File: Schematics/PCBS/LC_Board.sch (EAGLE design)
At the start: 21 parts, among them IC1 ATMEGA328P-AU, Q1 TRANSISTOR-FET_DMN2004K, Q10 220mA/50V/3.5Ω, Q2 TRANSISTOR-FET_DMN2004K, Q3 TRANSISTOR-FET_DMN2004K, Q4 TRANSISTOR-FET_DMN2004K, Q5 TRANSISTOR-FET_DMN2004K, Q6 TRANSISTOR-FET_DMN2004K, Q7 TRANSISTOR-FET_DMN2004K, Q8 TRANSISTOR-FET_DMN2004K, Q9 TRANSISTOR-FET_DMN2004K, U1 LT1763CS8-3.3#TRPBF

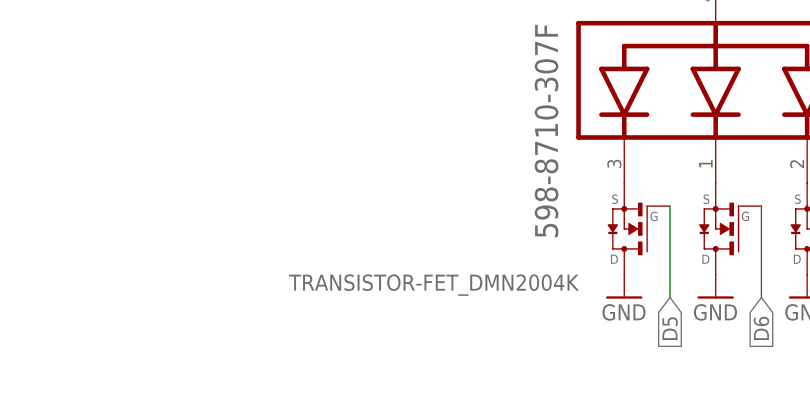
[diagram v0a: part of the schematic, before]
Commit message: update .gitignore && added MOSFET value to board
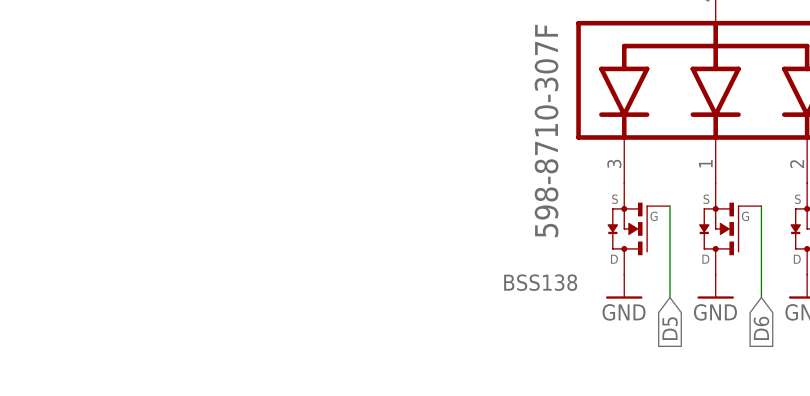
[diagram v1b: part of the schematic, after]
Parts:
- Q1, Q2, Q3, Q4, Q5, Q6, Q7, Q8, Q9: value TRANSISTOR-FET_DMN2004K -> BSS138
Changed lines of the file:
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@@
 <attribute name="SPICEPREFIX" value="E"/>
 </part>
-<part name="Q1" library="52101-101-REV-A" library_urn="urn:adsk.eagle:library:15662110" deviceset="TRANSISTOR-FET_DMN2004K" device="" package3d_urn="urn:adsk.eagle:package:15662287/2">
+<part name="Q1" library="52101-101-REV-A" library_urn="urn:adsk.eagle:library:15662110" deviceset="TRANSISTOR-FET_DMN2004K" device="" package3d_urn="urn:adsk.eagle:package:15662287/2" value="BSS138">
 <attribute name="SPICEPREFIX" value="Q"/>
 </part>
-<part name="Q2" library="52101-101-REV-A" library_urn="urn:adsk.eagle:library:15662110" deviceset="TRANSISTOR-FET_DMN2004K" device="" package3d_urn="urn:adsk.eagle:package:15662287/2">
+<part name="Q2" library="52101-101-REV-A" library_urn="urn:adsk.eagle:library:15662110" deviceset="TRANSISTOR-FET_DMN2004K" device="" package3d_urn="urn:adsk.eagle:package:15662287/2" value="BSS138">
 <attribute name="SPICEPREFIX" value="Q"/>
 </part>
-<part name="Q3" library="52101-101-REV-A" library_urn="urn:adsk.eagle:library:15662110" deviceset="TRANSISTOR-FET_DMN2004K" device="" package3d_urn="urn:adsk.eagle:package:15662287/2">
+<part name="Q3" library="52101-101-REV-A" library_urn="urn:adsk.eagle:library:15662110" deviceset="TRANSISTOR-FET_DMN2004K" device="" package3d_urn="urn:adsk.eagle:package:15662287/2" value="BSS138">
 <attribute name="SPICEPREFIX" value="Q"/>
 </part>
-<part name="Q4" library="52101-101-REV-A" library_urn="urn:adsk.eagle:library:15662110" deviceset="TRANSISTOR-FET_DMN2004K" device="" package3d_urn="urn:adsk.eagle:package:15662287/2">
+<part name="Q4" library="52101-101-REV-A" library_urn="urn:adsk.eagle:library:15662110" deviceset="TRANSISTOR-FET_DMN2004K" device="" package3d_urn="urn:adsk.eagle:package:15662287/2" value="BSS138">
 <attribute name="SPICEPREFIX" value="Q"/>
 </part>
-<part name="Q5" library="52101-101-REV-A" library_urn="urn:adsk.eagle:library:15662110" deviceset="TRANSISTOR-FET_DMN2004K" device="" package3d_urn="urn:adsk.eagle:package:15662287/2">
+<part name="Q5" library="52101-101-REV-A" library_urn="urn:adsk.eagle:library:15662110" deviceset="TRANSISTOR-FET_DMN2004K" device="" package3d_urn="urn:adsk.eagle:package:15662287/2" value="BSS138">
 <attribute name="SPICEPREFIX" value="Q"/>
 </part>
-<part name="Q6" library="52101-101-REV-A" library_urn="urn:adsk.eagle:library:15662110" deviceset="TRANSISTOR-FET_DMN2004K" device="" package3d_urn="urn:adsk.eagle:package:15662287/2">
+<part name="Q6" library="52101-101-REV-A" library_urn="urn:adsk.eagle:library:15662110" deviceset="TRANSISTOR-FET_DMN2004K" device="" package3d_urn="urn:adsk.eagle:package:15662287/2" value="BSS138">
 <attribute name="SPICEPREFIX" value="Q"/>
 </part>
-<part name="Q7" library="52101-101-REV-A" library_urn="urn:adsk.eagle:library:15662110" deviceset="TRANSISTOR-FET_DMN2004K" device="" package3d_urn="urn:adsk.eagle:package:15662287/2">
+<part name="Q7" library="52101-101-REV-A" library_urn="urn:adsk.eagle:library:15662110" deviceset="TRANSISTOR-FET_DMN2004K" device="" package3d_urn="urn:adsk.eagle:package:15662287/2" value="BSS138">
 <attribute name="SPICEPREFIX" value="Q"/>
 </part>
-<part name="Q8" library="52101-101-REV-A" library_urn="urn:adsk.eagle:library:15662110" deviceset="TRANSISTOR-FET_DMN2004K" device="" package3d_urn="urn:adsk.eagle:package:15662287/2">
+<part name="Q8" library="52101-101-REV-A" library_urn="urn:adsk.eagle:library:15662110" deviceset="TRANSISTOR-FET_DMN2004K" device="" package3d_urn="urn:adsk.eagle:package:15662287/2" value="BSS138">
 <attribute name="SPICEPREFIX" value="Q"/>
 </part>
-<part name="Q9" library="52101-101-REV-A" library_urn="urn:adsk.eagle:library:15662110" deviceset="TRANSISTOR-FET_DMN2004K" device="" package3d_urn="urn:adsk.eagle:package:15662287/2">
+<part name="Q9" library="52101-101-REV-A" library_urn="urn:adsk.eagle:library:15662110" deviceset="TRANSISTOR-FET_DMN2004K" device="" package3d_urn="urn:adsk.eagle:package:15662287/2" value="BSS138">
 <attribute name="SPICEPREFIX" value="Q"/>
 </part>

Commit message: updated IO
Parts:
- JP1: device adafruit:PINHD-1X8CLEANBIG -> pinhead:PINHD-1X8
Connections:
- new net RESET_IN: JP1.5
- net 2BD: no longer JP1.2
- net 3.3V_RAIL: now also JP1.4; no longer JP1.5
- net 5V_RAIL: now also JP1.3; no longer JP1.6
- net RXD_IN: now also JP1.6; no longer JP1.3
- net TXD: now also JP1.7; no longer JP1.4
- net VIN: now also JP1.2; no longer JP1.7
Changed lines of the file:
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@@
 <part name="R3" library="SparkFun-Resistors" deviceset="10OHM" device="-HORIZ-1/4W-1%" value="10K"/>
 <part name="Q10" library="SparkFun-DiscreteSemi" deviceset="MOSFET-NCH" device="-BSS138" value="220mA/50V/3.5Ω"/>
-<part name="JP1" library="adafruit" library_urn="urn:adsk.eagle:library:420" deviceset="PINHD-1X8" device="CLEANBIG" package3d_urn="urn:adsk.eagle:package:6240708/1"/>
 <part name="E1" library="52101-101-REV-A" library_urn="urn:adsk.eagle:library:15662110" deviceset="DPADS_PAD" device="-0400-S" package3d_urn="urn:adsk.eagle:package:15662248/2"/>
 <part name="E2" library="52101-101-REV-A" library_urn="urn:adsk.eagle:library:15662110" deviceset="DPADS_PAD" device="-0400-S" package3d_urn="urn:adsk.eagle:package:15662248/2"/>
+<part name="JP1" library="pinhead" library_urn="urn:adsk.eagle:library:325" deviceset="PINHD-1X8" device="" package3d_urn="urn:adsk.eagle:package:22409/2"/>
 </parts>
 <sheets>
@@
 </instance>
 <instance part="Q10" gate="NMOS" x="452.12" y="2.54" smashed="yes" rot="R90"/>
-<instance part="JP1" gate="G$1" x="449.58" y="30.48" smashed="yes" rot="R180">
+<instance part="E1" gate="P" x="558.8" y="33.02" smashed="yes" rot="R180">
+<attribute name="NAME" x="556.895" y="33.9725" size="1.778" layer="95" rot="R180"/>
+</instance>
+<instance part="E2" gate="P" x="558.8" y="30.48" smashed="yes" rot="R180">
+<attribute name="NAME" x="556.895" y="31.4325" size="1.778" layer="95" rot="R180"/>
+</instance>
+<instance part="JP1" gate="A" x="449.58" y="33.02" smashed="yes" rot="R180">
 <attribute name="NAME" x="455.93" y="19.685" size="1.778" layer="95" rot="R180"/>
 <attribute name="VALUE" x="455.93" y="45.72" size="1.778" layer="96" rot="R180"/>
-</instance>
-<instance part="E1" gate="P" x="558.8" y="33.02" smashed="yes" rot="R180">
-<attribute name="NAME" x="556.895" y="33.9725" size="1.778" layer="95" rot="R180"/>
-</instance>
-<instance part="E2" gate="P" x="558.8" y="30.48" smashed="yes" rot="R180">
-<attribute name="NAME" x="556.895" y="31.4325" size="1.778" layer="95" rot="R180"/>
 </instance>
 </instances>
@@
 </segment>
 <segment>
-<wire x1="452.12" y1="33.02" x2="457.2" y2="33.02" width="0.1524" layer="91"/>
-<label x="457.2" y="33.02" size="0.5588" layer="95" xref="yes"/>
-<pinref part="JP1" gate="G$1" pin="5"/>
+<wire x1="452.12" y1="30.48" x2="457.2" y2="30.48" width="0.1524" layer="91"/>
+<label x="457.2" y="30.48" size="0.5588" layer="95" xref="yes"/>
+<pinref part="JP1" gate="A" pin="4"/>
 </segment>
 </net>
@@
 <pinref part="GND18" gate="1" pin="GND"/>
 <wire x1="452.12" y1="40.64" x2="459.74" y2="40.64" width="0.1524" layer="91"/>
-<pinref part="JP1" gate="G$1" pin="8"/>
+<pinref part="JP1" gate="A" pin="8"/>
 </segment>
 <segment>
@@
 <net name="VIN" class="0">
 <segment>
-<wire x1="452.12" y1="38.1" x2="457.2" y2="38.1" width="0.1524" layer="91"/>
-<label x="457.2" y="38.1" size="0.6096" layer="95" xref="yes"/>
-<pinref part="JP1" gate="G$1" pin="7"/>
+<wire x1="452.12" y1="25.4" x2="457.2" y2="25.4" width="0.1524" layer="91"/>
+<label x="457.2" y="25.4" size="0.6096" layer="95" xref="yes"/>
+<pinref part="JP1" gate="A" pin="2"/>
 </segment>
 <segment>
@@
 </segment>
 <segment>
-<wire x1="452.12" y1="30.48" x2="457.2" y2="30.48" width="0.1524" layer="91"/>
-<label x="457.2" y="30.48" size="0.6096" layer="95" xref="yes"/>
-<pinref part="JP1" gate="G$1" pin="4"/>
+<wire x1="452.12" y1="38.1" x2="457.2" y2="38.1" width="0.1524" layer="91"/>
+<label x="457.2" y="38.1" size="0.6096" layer="95" xref="yes"/>
+<pinref part="JP1" gate="A" pin="7"/>
 </segment>
 </net>
@@
 <net name="RXD_IN" class="0">
 <segment>
-<wire x1="452.12" y1="27.94" x2="457.2" y2="27.94" width="0.1524" layer="91"/>
-<label x="457.2" y="27.94" size="0.6096" layer="95" xref="yes"/>
-<pinref part="JP1" gate="G$1" pin="3"/>
+<wire x1="452.12" y1="35.56" x2="457.2" y2="35.56" width="0.1524" layer="91"/>
+<label x="457.2" y="35.56" size="0.6096" layer="95" xref="yes"/>
+<pinref part="JP1" gate="A" pin="6"/>
 </segment>
 <segment>
@@
 <net name="5V_RAIL" class="0">
 <segment>
-<wire x1="452.12" y1="35.56" x2="457.2" y2="35.56" width="0.1524" layer="91"/>
-<label x="457.2" y="35.56" size="0.5588" layer="95" xref="yes"/>
-<pinref part="JP1" gate="G$1" pin="6"/>
+<wire x1="452.12" y1="27.94" x2="457.2" y2="27.94" width="0.1524" layer="91"/>
+<label x="457.2" y="27.94" size="0.5588" layer="95" xref="yes"/>
+<pinref part="JP1" gate="A" pin="3"/>
 </segment>
 </net>
 <net name="2BD" class="0">
-<segment>
-<wire x1="452.12" y1="25.4" x2="457.2" y2="25.4" width="0.1524" layer="91"/>
-<label x="457.2" y="25.4" size="0.5588" layer="95" xref="yes"/>
-<pinref part="JP1" gate="G$1" pin="2"/>
-</segment>
 <segment>
 <wire x1="452.12" y1="22.86" x2="457.2" y2="22.86" width="0.1524" layer="91"/>
 <label x="457.2" y="22.86" size="0.5588" layer="95" xref="yes"/>
-<pinref part="JP1" gate="G$1" pin="1"/>
-</segment>
-</net>
+<pinref part="JP1" gate="A" pin="1"/>
+</segment>
+</net>
+<net name="RESET_IN" class="0">
+<segment>
+<wire x1="452.12" y1="33.02" x2="457.2" y2="33.02" width="0.1524" layer="91"/>
+<label x="457.2" y="33.02" size="0.5588" layer="95" xref="yes"/>
+<pinref part="JP1" gate="A" pin="5"/>
+</segment>
+</net>

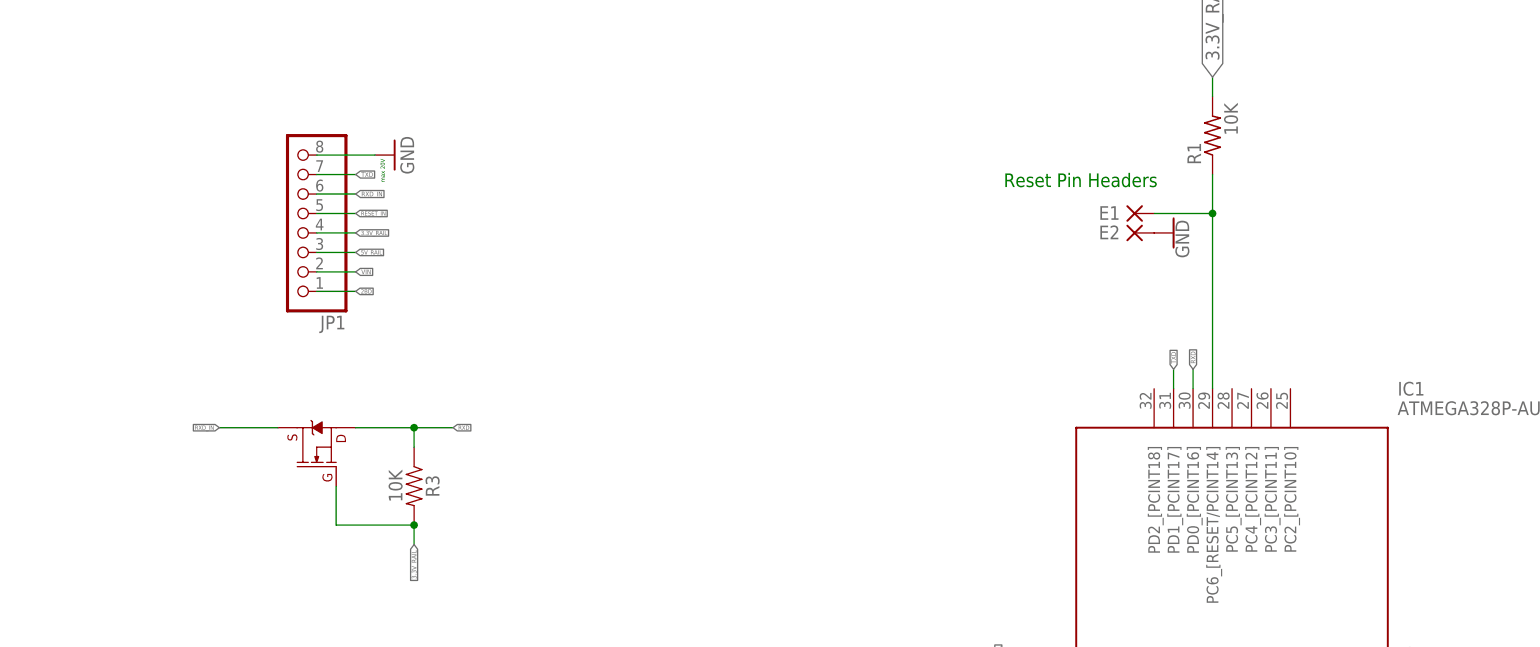
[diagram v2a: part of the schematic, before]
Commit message: 3.3v && 5v selcetor headers added
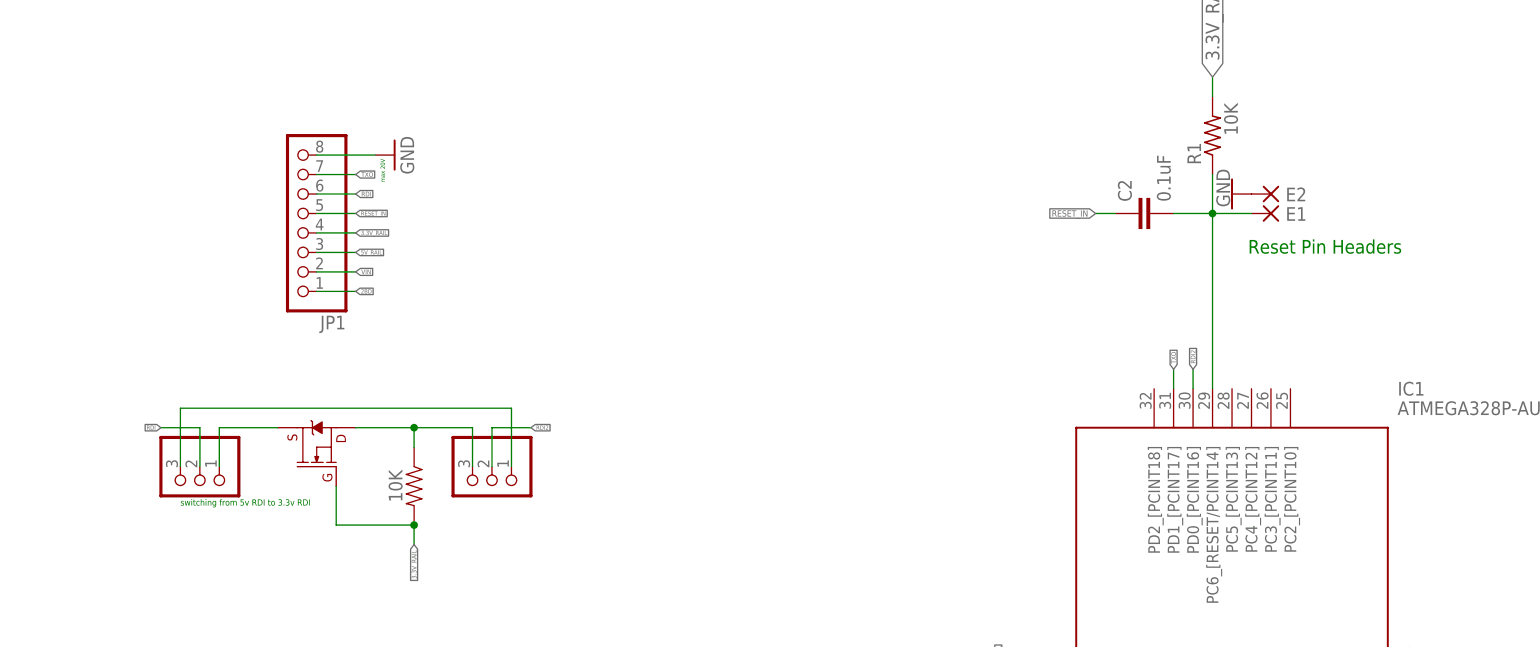
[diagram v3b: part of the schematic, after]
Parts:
- added C2: 0.1uF, SparkFun-Capacitors:0.1UF-0603-25V-(+80/-20%)
- added JP2, JP3: (no value), pinhead:PINHD-1X3
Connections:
- net TXD renamed TXO
- removed net RXD: IC1.PD0_[PCINT16], Q10.S, R3.1
- new net RDI: JP1.6, JP2.2, JP2.3, JP3.1
- new net RDI2: IC1.PD0_[PCINT16], JP3.2
- new net RXI2: JP3.3, Q10.S, R3.1
- net N$15: now also C2.2
- net RESET_IN: now also C2.1
- net RXD_IN: now also JP2.1; no longer JP1.6
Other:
- note added: "switching from 5v RDI to 3.3v RDI"
- moved on the sheet: E1, E2

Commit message: added lables to 5v to 3.3v on RXI
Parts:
- JP1: value (none) -> IO
- JP2: value (none) -> switching from 5v RDI to 3.3v RDI input
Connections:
- new net RDI_3.3V: JP2.3, JP3.1
- net RDI: no longer JP2.3, JP3.1
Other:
- note removed: "switching from 5v RDI to 3.3v RDI"
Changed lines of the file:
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@@
 <part name="E1" library="52101-101-REV-A" library_urn="urn:adsk.eagle:library:15662110" deviceset="DPADS_PAD" device="-0400-S" package3d_urn="urn:adsk.eagle:package:15662248/2"/>
 <part name="E2" library="52101-101-REV-A" library_urn="urn:adsk.eagle:library:15662110" deviceset="DPADS_PAD" device="-0400-S" package3d_urn="urn:adsk.eagle:package:15662248/2"/>
-<part name="JP1" library="pinhead" library_urn="urn:adsk.eagle:library:325" deviceset="PINHD-1X8" device="" package3d_urn="urn:adsk.eagle:package:22409/2"/>
+<part name="JP1" library="pinhead" library_urn="urn:adsk.eagle:library:325" deviceset="PINHD-1X8" device="" package3d_urn="urn:adsk.eagle:package:22409/2" value="IO"/>
 <part name="C2" library="SparkFun-Capacitors" library_urn="urn:adsk.eagle:library:510" deviceset="0.1UF" device="-0603-25V-(+80/-20%)" package3d_urn="urn:adsk.eagle:package:37414/1" value="0.1uF"/>
-<part name="JP2" library="pinhead" library_urn="urn:adsk.eagle:library:325" deviceset="PINHD-1X3" device="" package3d_urn="urn:adsk.eagle:package:22458/2"/>
+<part name="JP2" library="pinhead" library_urn="urn:adsk.eagle:library:325" deviceset="PINHD-1X3" device="" package3d_urn="urn:adsk.eagle:package:22458/2" value="switching from 5v RDI to 3.3v RDI input"/>
 <part name="JP3" library="pinhead" library_urn="urn:adsk.eagle:library:325" deviceset="PINHD-1X3" device="" package3d_urn="urn:adsk.eagle:package:22458/2"/>
 </parts>
@@
 <text x="593.67" y="29.57" size="1.778" layer="91" rot="R180">Reset Pin Headers</text>
 <text x="461.01" y="37.084" size="0.5588" layer="91" rot="R90">max 20V</text>
-<text x="434.34" y="-5.08" size="0.8128" layer="91">switching from 5v RDI to 3.3v RDI</text>
 </plain>
 <instances>
@@
 </instance>
 <instance part="JP1" gate="A" x="449.58" y="33.02" smashed="yes" rot="R180">
-<attribute name="NAME" x="455.93" y="19.685" size="1.778" layer="95" rot="R180"/>
 <attribute name="VALUE" x="455.93" y="45.72" size="1.778" layer="96" rot="R180"/>
 </instance>
@@
 </instance>
 <instance part="JP2" gate="A" x="436.88" y="-2.54" smashed="yes" rot="R270">
-<attribute name="VALUE" x="429.26" y="3.81" size="1.778" layer="96" rot="R270"/>
+<attribute name="VALUE" x="448.31" y="-5.08" size="0.8128" layer="96" rot="R180"/>
 </instance>
 <instance part="JP3" gate="A" x="474.98" y="-2.54" smashed="yes" rot="R270">
@@
 </segment>
 <segment>
-<pinref part="JP2" gate="A" pin="3"/>
-<wire x1="434.34" y1="7.62" x2="434.34" y2="0" width="0.1524" layer="91"/>
-<wire x1="434.34" y1="7.62" x2="477.52" y2="7.62" width="0.1524" layer="91"/>
-<pinref part="JP3" gate="A" pin="1"/>
-<wire x1="477.52" y1="7.62" x2="477.52" y2="0" width="0.1524" layer="91"/>
-</segment>
-<segment>
 <pinref part="JP2" gate="A" pin="2"/>
 <wire x1="436.88" y1="5.08" x2="436.88" y2="0" width="0.1524" layer="91"/>
@@
 </segment>
 </net>
+<net name="RDI_3.3V" class="0">
+<segment>
+<pinref part="JP2" gate="A" pin="3"/>
+<wire x1="434.34" y1="7.62" x2="434.34" y2="0" width="0.1524" layer="91"/>
+<wire x1="434.34" y1="7.62" x2="477.52" y2="7.62" width="0.1524" layer="91"/>
+<pinref part="JP3" gate="A" pin="1"/>
+<wire x1="477.52" y1="7.62" x2="477.52" y2="0" width="0.1524" layer="91"/>
+<label x="434.34" y="7.62" size="0.8128" layer="95"/>
+</segment>
+</net>

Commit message: Added lables to LC_board led gnd control mostfets
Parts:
- renumbered Q1 to LED1RED, Q2 to LED1GREEN, Q3 to LED1BLUE, Q4 to LED2RED, Q5 to LED2GREEN, Q6 to LED2BLUE, Q7 to LED3RED, Q8 to LED3GREEN, Q9 to LED3BLUE
